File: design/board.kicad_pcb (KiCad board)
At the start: 2 copper layers, 37 parts, among them J1 Conn_02x06_Odd_Even, SW1 SW_Push, SW2 SW_Push, SW3 SW_Push, SW4 SW_Push, SW5 SW_Push, SW6 SW_Push, U1 LM555, U2 LM555, U3 LM555, U4 LM555, U5 LM555, U6 LM555

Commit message: PCB layout.
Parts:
- C1, C10, C11, C12, C2, C3, C4, C5, C6, C7, C8, C9, R1, R10, R11, R12, R2, R3, R4, R5, R6, R7, R8, R9, U1, U2, U3, U4, U5, U6: moved to B.Cu
- J1: value Conn_02x06_Odd_Even -> Conn_02x04_Odd_Even; footprint Connector_PinHeader_2.54mm:PinHeader_2x06_P2.54mm_Vertical -> Connector_PinSocket_2.54mm:PinSocket_2x04_P2.54mm_Vertical
- moved R12 110.8 mm to (146.7, 135.0), turned to 90 degrees
- moved R11 109.0 mm to (146.7, 129.0), turned to 270 degrees
- moved R10 106.0 mm to (134.7, 147.0), turned to 90 degrees
- moved R9 104.1 mm to (134.7, 141.0), turned to 270 degrees
- moved SW6 102.9 mm to (150.8, 131.7)
- moved U6 102.7 mm to (150.8, 131.7), turned to 270 degrees
- moved C11 101.1 mm to (155.3, 135.0), turned to 90 degrees
- moved SW5 98.3 mm to (138.8, 143.7)
- moved U5 97.8 mm to (138.8, 143.7), turned to 270 degrees
- moved C9 97.3 mm to (143.3, 146.9), turned to 90 degrees
- moved R8 96.2 mm to (110.7, 147.0), turned to 90 degrees
- moved C7 94.6 mm to (119.3, 147.0), turned to 90 degrees
- moved C8 93.0 mm to (119.3, 141.0), turned to 270 degrees
- moved SW4 93.0 mm to (114.8, 143.7)
- moved U4 92.9 mm to (114.8, 143.7)
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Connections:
- net Net-(C1-Pad2) renamed /L_5
- net Net-(C10-Pad2) renamed /A_67
- net Net-(C11-Pad2) renamed /B_5
- net Net-(C12-Pad2) renamed /B_67
- net Net-(C2-Pad2) renamed /L_67
- net Net-(C3-Pad2) renamed /U_5
- net Net-(C4-Pad2) renamed /U_67
- net Net-(C5-Pad2) renamed /R_5
- net Net-(C6-Pad2) renamed /R_67
- net Net-(C7-Pad2) renamed /D_5
- net Net-(C8-Pad2) renamed /D_67
- net Net-(C9-Pad2) renamed /A_5
- net Net-(J1-Pad3) renamed /L_out
- net Net-(J1-Pad4) renamed /U_out
- J1 pad 5: Net-(J1-Pad5) -> /R_out
- J1 pad 6: Net-(J1-Pad6) -> /D_out
- J1 pad 7: Net-(J1-Pad7) -> /A_out
- J1 pad 8: Net-(J1-Pad8) -> /B_out
- R1 pad 2: Net-(R1-Pad2) -> /L_button
- R11 pad 2: Net-(R11-Pad2) -> /B_button
- R3 pad 2: Net-(R3-Pad2) -> /U_button
- R5 pad 2: Net-(R5-Pad2) -> /R_button
- R7 pad 2: Net-(R7-Pad2) -> /D_button
- R9 pad 2: Net-(R9-Pad2) -> /A_button
- SW1 pad 2: Net-(R1-Pad2) -> /L_button
- SW1 pad 3: (no net) -> /VCC
- SW1 pad 4: (no net) -> /L_button
- SW2 pad 2: Net-(R3-Pad2) -> /U_button
- SW2 pad 3: (no net) -> /VCC
- SW2 pad 4: (no net) -> /U_button
- SW3 pad 2: Net-(R5-Pad2) -> /R_button
- SW3 pad 3: (no net) -> /VCC
- SW3 pad 4: (no net) -> /R_button
- SW4 pad 2: Net-(R7-Pad2) -> /D_button
- SW4 pad 3: (no net) -> /VCC
- SW4 pad 4: (no net) -> /D_button
- SW5 pad 2: Net-(R9-Pad2) -> /A_button
- SW5 pad 3: (no net) -> /VCC
- SW5 pad 4: (no net) -> /A_button
- SW6 pad 2: Net-(R11-Pad2) -> /B_button
- SW6 pad 3: (no net) -> /VCC
- SW6 pad 4: (no net) -> /B_button
- U1 pad 2: Net-(R1-Pad2) -> /L_button
- U2 pad 2: Net-(R3-Pad2) -> /U_button
- U3 pad 2: Net-(R5-Pad2) -> /R_button
- U3 pad 3: Net-(J1-Pad7) -> /R_out
- U4 pad 2: Net-(R7-Pad2) -> /D_button
- U4 pad 3: Net-(J1-Pad8) -> /D_out
- U5 pad 2: Net-(R9-Pad2) -> /A_button
- U5 pad 3: Net-(J1-Pad9) -> /A_out
- U6 pad 2: Net-(R11-Pad2) -> /B_button
- U6 pad 3: Net-(J1-Pad10) -> /B_out
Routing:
- net /VCC: track 0.00 -> 73.6 mm
- net /A_button: track 0.00 -> 25.6 mm
- net /R_button: track 0.00 -> 25.6 mm
- net /B_button: track 0.00 -> 25.6 mm
- net /D_button: track 0.00 -> 25.6 mm
- net /L_button: track 0.00 -> 25.6 mm
- net /U_button: track 0.00 -> 25.6 mm
- net /R_67: track 0.00 -> 12.5 mm
- net /U_67: track 0.00 -> 12.3 mm
- net /A_67: track 0.00 -> 12.3 mm
- net /D_67: track 0.00 -> 12.3 mm
- net /B_67: track 0.00 -> 12.3 mm
- net /L_67: track 0.00 -> 12.2 mm
- net /U_out: track 0.00 -> 5.83 mm, vias 0 -> 1
- net /A_out: track 0.00 -> 4.78 mm, vias 0 -> 1
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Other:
- board outline added: 123.4 x 53.2 mm
- board text added: ".01"
- board text added: ".1"
- board text added: "1K"
- board text added: "1M"

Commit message: v1 of the controller done.
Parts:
- J1: moved to B.Cu
- moved C7 112.0 mm to (52.8, 56.9)
- moved R8 112.0 mm to (44.2, 56.9)
- moved SW1 112.0 mm to (36.3, 41.6)
- moved SW3 112.0 mm to (60.3, 41.6)
- moved SW4 112.0 mm to (48.3, 53.6)
- moved U4 112.0 mm to (48.3, 53.6)
- moved C1 112.0 mm to (40.8, 44.8)
- moved C2 112.0 mm to (40.8, 38.9)
- moved C3 112.0 mm to (52.8, 32.9)
- moved C4 112.0 mm to (52.8, 26.9)
- moved C5 112.0 mm to (64.8, 44.9)
- moved C6 112.0 mm to (64.8, 39.0)
- moved C8 112.0 mm to (52.8, 50.9)
- moved R1 112.0 mm to (32.2, 38.9)
- moved R2 112.0 mm to (32.2, 44.9)
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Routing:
- net /L_out: track 4.14 -> 87.4 mm
- net /D_out: track 4.69 -> 77.6 mm
- net /U_out: track 5.83 -> 60.4 mm
- net /R_out: track 4.71 -> 53.4 mm
- net /A_out: track 4.78 -> 27.2 mm
- net /B_out: track 4.57 -> 26.3 mm
- added copper zone on B.Cu, net /GND
- added copper zone on F.Cu, net /VCC
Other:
- board size 123.4 x 53.2 mm -> 120 x 50 mm
- board text added: "<-"
- board text added: "A"
- board text added: "B"
- board text added: "DOWN"
- board text added: "GND"
- board text added: "I/O ports"
- board text added: "LEFT"
- board text added: "RIGHT"
- board text added: "UP"
- board text added: "VCC"

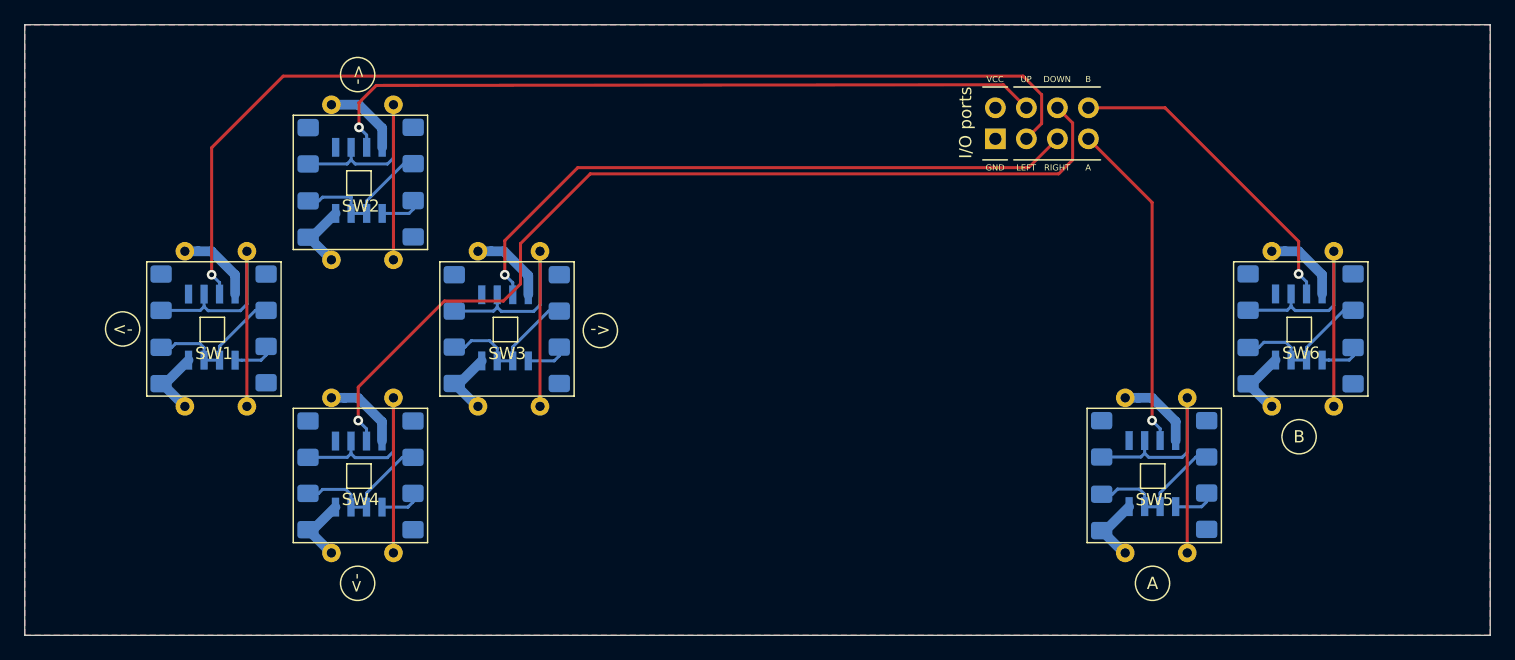
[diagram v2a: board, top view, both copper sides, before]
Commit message: New decoupling capacitor + mounting holes + image update.
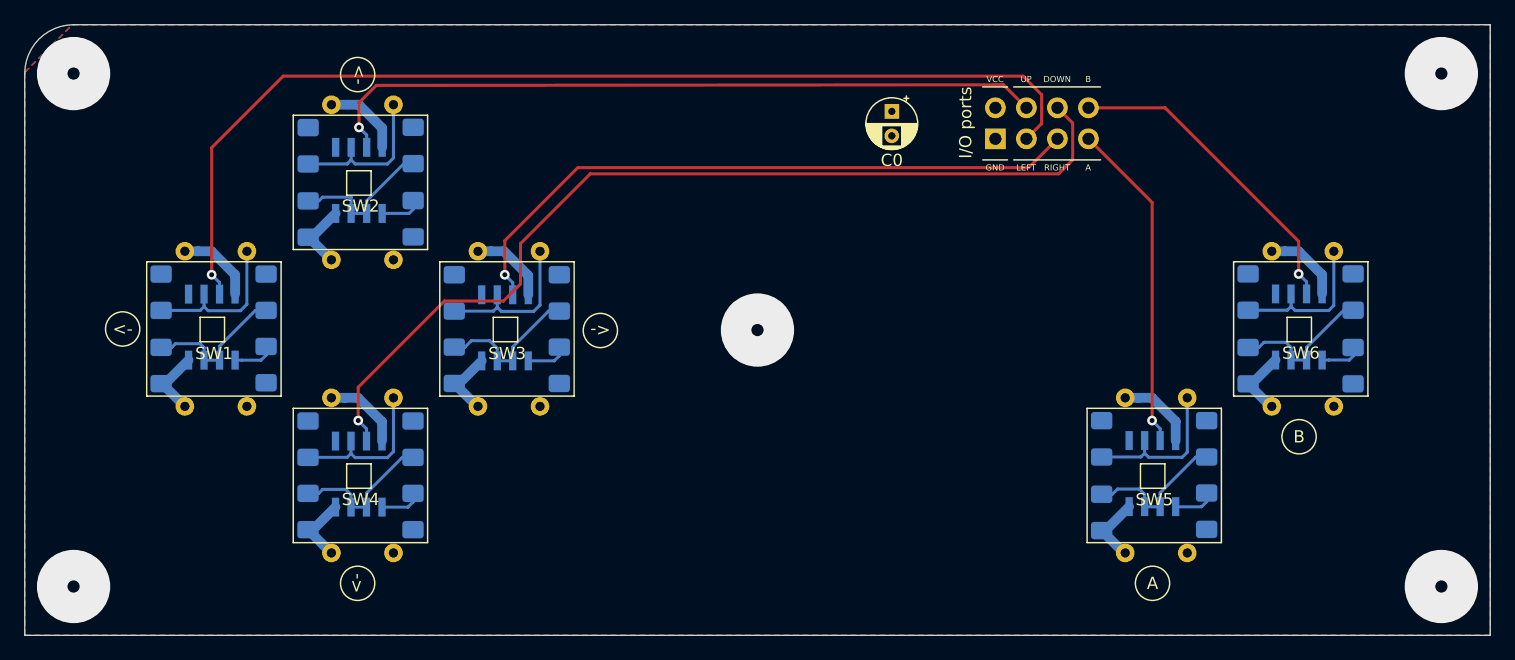
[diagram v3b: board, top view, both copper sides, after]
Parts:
- added C0: CP, Capacitor_THT:CP_Radial_D4.0mm_P2.00mm, F.Cu at (92.0, 24.1)
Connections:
- SW1 pad 4: /L_button -> (no net)
- SW2 pad 4: /U_button -> (no net)
- SW3 pad 4: /R_button -> (no net)
- SW4 pad 4: /D_button -> (no net)
- SW5 pad 4: /A_button -> (no net)
- SW6 pad 4: /B_button -> (no net)
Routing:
- net /L_button: track 25.6 -> 12.9 mm
- net /D_button: track 25.6 -> 12.9 mm
- net /A_button: track 25.6 -> 12.9 mm
- net /R_button: track 25.6 -> 12.9 mm
- net /B_button: track 25.6 -> 12.9 mm
- net /U_button: track 25.6 -> 12.9 mm
- net (no net): vias 0 -> 5
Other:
- outline, holes or cut-outs redrawn
